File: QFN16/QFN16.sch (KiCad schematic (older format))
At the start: 4 parts, among them J1 Conn_01x08, J2 Conn_02x08_Counter_Clockwise, J3 Conn_01x08, J4 Conn_02x08_Counter_Clockwise

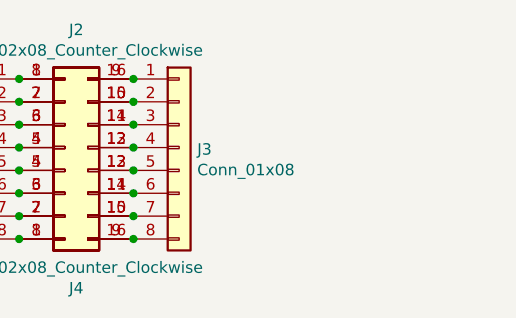
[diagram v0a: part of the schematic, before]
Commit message: Silkscreens and sizes updated
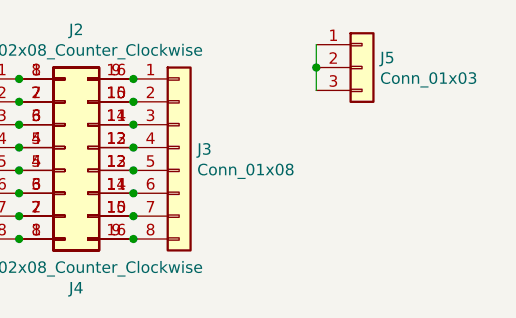
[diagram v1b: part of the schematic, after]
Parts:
- added J5: Conn_01x03, Connector_PinHeader_2.54mm:PinHeader_1x03_P2.54mm_Vertical, symbol Connector_Generic:Conn_01x03
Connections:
- new net: J5.1 (Pin_1), J5.2 (Pin_2), J5.3 (Pin_3)
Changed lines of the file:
@@
 Connection ~ 5800 3950
 Connection ~ 5800 4050
+$Comp
+L Connector_Generic:Conn_01x03 J5
+U 1 1 5D3B084D
+P 6800 3300
+F 0 "J5" H 6879 3342 50  0000 L CNN
+F 1 "Conn_01x03" H 6879 3252 50  0000 L CNN
+F 2 "Connector_PinHeader_2.54mm:PinHeader_1x03_P2.54mm_Vertical" H 6800 3300 50  0001 C CNN
+F 3 "~" H 6800 3300 50  0001 C CNN
+	1    6800 3300
+	1    0    0    -1
+$EndComp
+Wire Wire Line
+	6600 3200 6600 3300
+Connection ~ 6600 3300
+Wire Wire Line
+	6600 3300 6600 3400
 $EndSCHEMATC

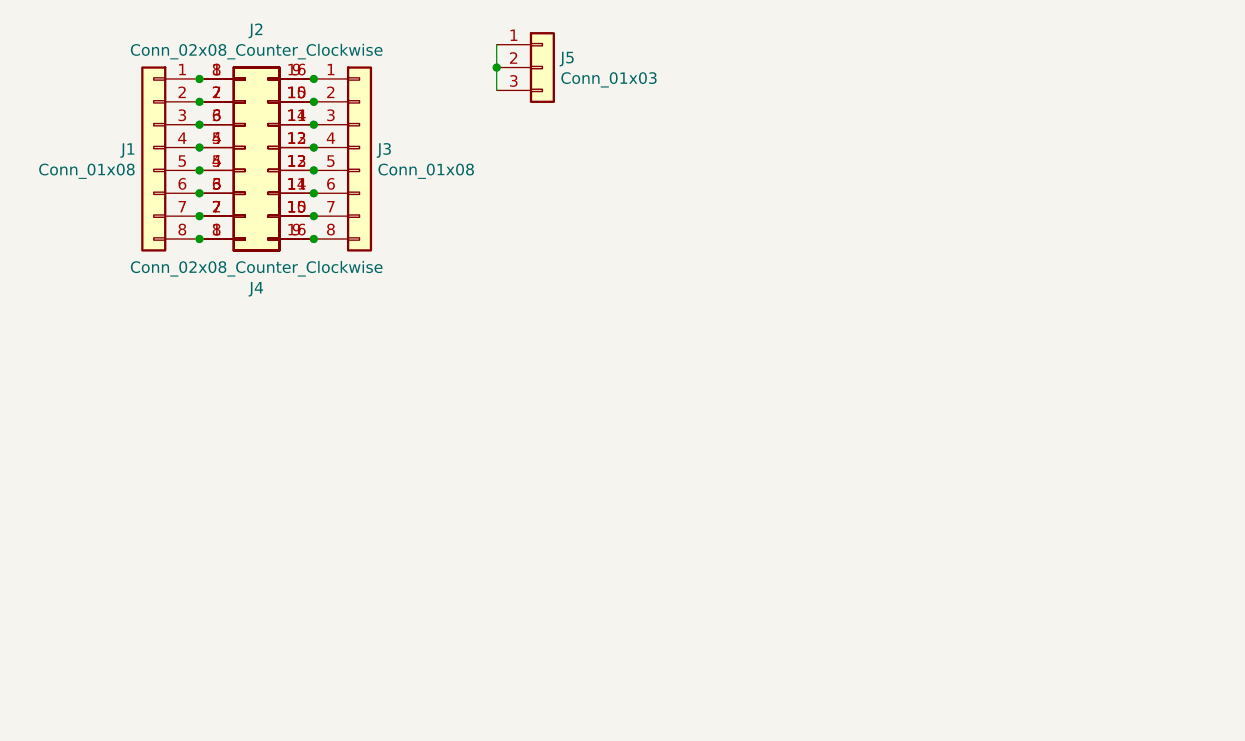
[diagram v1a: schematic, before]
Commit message: USB, SD and CR Cells Added
MicroSD, MicroUSB, MiniUSB, USB-C, CR1220, CR2032 added as well as all schematics page sizes optimised
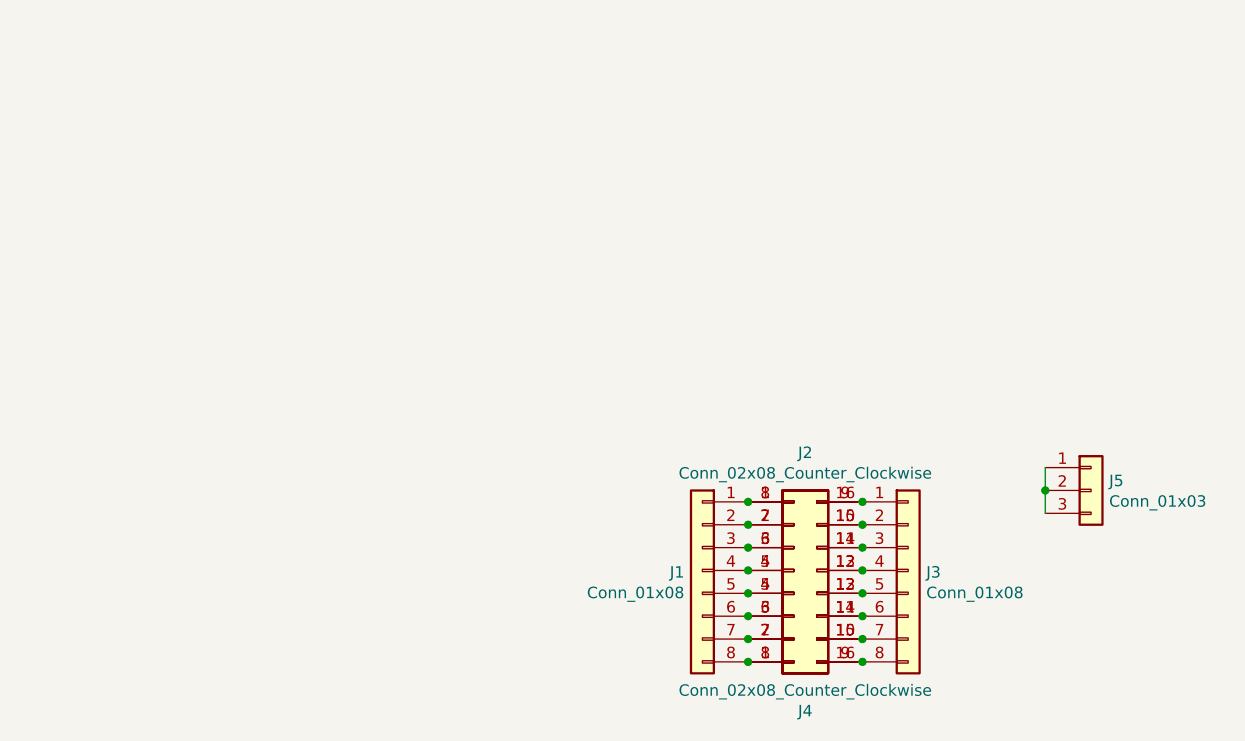
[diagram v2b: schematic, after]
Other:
- moved on the sheet: J1, J2, J3, J4, J5
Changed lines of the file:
@@
 encoding utf-8
 Sheet 1 1
-Title ""
-Date ""
-Rev ""
-Comp ""
-Comment1 ""
-Comment2 ""
-Comment3 ""
+Title "QFN16 to DIP Breakout Board"
+Date "2019-07-11"
+Rev "1"
+Comp "SirBoard"
+Comment1 "QFN16 P = 0.5mm"
+Comment2 "QFN16 P = 0.8mm"
+Comment3 "DIP16 P = 2.54mm"
 Comment4 ""
 $EndDescr
@@
 L Connector_Generic:Conn_01x08 J3
 U 1 1 5D27708E
-P 6000 3650
-F 0 "J3" H 6079 3642 50  0000 L CNN
-F 1 "Conn_01x08" H 6079 3552 50  0000 L CNN
-F 2 "Connector_PinHeader_2.54mm:PinHeader_1x08_P2.54mm_Vertical" H 6000 3650 50  0001 C CNN
-F 3 "~" H 6000 3650 50  0001 C CNN
-	1    6000 3650
+P 8400 5500
+F 0 "J3" H 8479 5492 50  0000 L CNN
+F 1 "Conn_01x08" H 8479 5402 50  0000 L CNN
+F 2 "Connector_PinHeader_2.54mm:PinHeader_1x08_P2.54mm_Vertical" H 8400 5500 50  0001 C CNN
+F 3 "~" H 8400 5500 50  0001 C CNN
+	1    8400 5500
 	1    0    0    -1
 $EndComp
@@
 L Connector_Generic:Conn_02x08_Counter_Clockwise J2
 U 1 1 5D2772F5
-P 5500 3650
-F 0 "J2" H 5550 4165 50  0000 C CNN
-F 1 "Conn_02x08_Counter_Clockwise" H 5550 4075 50  0000 C CNN
-F 2 "Package_DFN_QFN:QFN-20-1EP_4x4mm_P0.5mm_EP2.7x2.7mm" H 5500 3650 50  0001 C CNN
-F 3 "~" H 5500 3650 50  0001 C CNN
-	1    5500 3650
+P 7900 5500
+F 0 "J2" H 7950 6015 50  0000 C CNN
+F 1 "Conn_02x08_Counter_Clockwise" H 7950 5925 50  0000 C CNN
+F 2 "Package_DFN_QFN:QFN-20-1EP_4x4mm_P0.5mm_EP2.7x2.7mm" H 7900 5500 50  0001 C CNN
+F 3 "~" H 7900 5500 50  0001 C CNN
+	1    7900 5500
 	1    0    0    -1
 $EndComp
@@
 L Connector_Generic:Conn_01x08 J1
 U 1 1 5D27904E
-P 5100 3650
-F 0 "J1" H 5179 3642 50  0000 L CNN
-F 1 "Conn_01x08" H 5179 3552 50  0000 L CNN
-F 2 "Connector_PinHeader_2.54mm:PinHeader_1x08_P2.54mm_Vertical" H 5100 3650 50  0001 C CNN
-F 3 "~" H 5100 3650 50  0001 C CNN
-	1    5100 3650
+P 7500 5500
+F 0 "J1" H 7579 5492 50  0000 L CNN
+F 1 "Conn_01x08" H 7579 5402 50  0000 L CNN
+F 2 "Connector_PinHeader_2.54mm:PinHeader_1x08_P2.54mm_Vertical" H 7500 5500 50  0001 C CNN
+F 3 "~" H 7500 5500 50  0001 C CNN
+	1    7500 5500
 	-1   0    0    -1
 $EndComp
@@
 L Connector_Generic:Conn_02x08_Counter_Clockwise J4
 U 1 1 5D27A0A0
-P 5500 3750
-F 0 "J4" H 5550 4265 50  0000 C CNN
-F 1 "Conn_02x08_Counter_Clockwise" H 5550 4175 50  0000 C CNN
-F 2 "Package_DFN_QFN:QFN-16-1EP_5x5mm_P0.8mm_EP2.7x2.7mm" H 5500 3750 50  0001 C CNN
-F 3 "~" H 5500 3750 50  0001 C CNN
-	1    5500 3750
+P 7900 5600
+F 0 "J4" H 7950 6115 50  0000 C CNN
+F 1 "Conn_02x08_Counter_Clockwise" H 7950 6025 50  0000 C CNN
+F 2 "Package_DFN_QFN:QFN-16-1EP_5x5mm_P0.8mm_EP2.7x2.7mm" H 7900 5600 50  0001 C CNN
+F 3 "~" H 7900 5600 50  0001 C CNN
+	1    7900 5600
 	1    0    0    1
 $EndComp
-Connection ~ 5300 3350
-Connection ~ 5300 3450
-Connection ~ 5300 3550
-Connection ~ 5300 3650
-Connection ~ 5300 3750
-Connection ~ 5300 3850
-Connection ~ 5300 3950
-Connection ~ 5300 4050
-Connection ~ 5800 3350
-Connection ~ 5800 3450
-Connection ~ 5800 3550
-Connection ~ 5800 3650
-Connection ~ 5800 3750
-Connection ~ 5800 3850
-Connection ~ 5800 3950
-Connection ~ 5800 4050
+Connection ~ 7700 5200
+Connection ~ 7700 5300
+Connection ~ 7700 5400
+Connection ~ 7700 5500
+Connection ~ 7700 5600
+Connection ~ 7700 5700
+Connection ~ 7700 5800
+Connection ~ 7700 5900
+Connection ~ 8200 5200
+Connection ~ 8200 5300
+Connection ~ 8200 5400
+Connection ~ 8200 5500
+Connection ~ 8200 5600
+Connection ~ 8200 5700
+Connection ~ 8200 5800
+Connection ~ 8200 5900
 $Comp
 L Connector_Generic:Conn_01x03 J5
 U 1 1 5D3B084D
-P 6800 3300
-F 0 "J5" H 6879 3342 50  0000 L CNN
-F 1 "Conn_01x03" H 6879 3252 50  0000 L CNN
-F 2 "Connector_PinHeader_2.54mm:PinHeader_1x03_P2.54mm_Vertical" H 6800 3300 50  0001 C CNN
-F 3 "~" H 6800 3300 50  0001 C CNN
-	1    6800 3300
+P 9200 5150
+F 0 "J5" H 9279 5192 50  0000 L CNN
+F 1 "Conn_01x03" H 9279 5102 50  0000 L CNN
+F 2 "Connector_PinHeader_2.54mm:PinHeader_1x03_P2.54mm_Vertical" H 9200 5150 50  0001 C CNN
+F 3 "~" H 9200 5150 50  0001 C CNN
+	1    9200 5150
 	1    0    0    -1
 $EndComp
 Wire Wire Line
-	6600 3200 6600 3300
-Connection ~ 6600 3300
+	9000 5050 9000 5150
+Connection ~ 9000 5150
 Wire Wire Line
-	6600 3300 6600 3400
+	9000 5150 9000 5250
 $EndSCHEMATC

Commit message: Page Settings Updated
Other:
- moved on the sheet: J1, J2, J3, J4, J5
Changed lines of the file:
@@
 EELAYER 29 0
 EELAYER END
-$Descr A4 11693 8268
+$Descr User 8268 5807
 encoding utf-8
 Sheet 1 1
@@
 L Connector_Generic:Conn_01x08 J3
 U 1 1 5D27708E
-P 8400 5500
-F 0 "J3" H 8479 5492 50  0000 L CNN
-F 1 "Conn_01x08" H 8479 5402 50  0000 L CNN
-F 2 "Connector_PinHeader_2.54mm:PinHeader_1x08_P2.54mm_Vertical" H 8400 5500 50  0001 C CNN
-F 3 "~" H 8400 5500 50  0001 C CNN
-	1    8400 5500
+P 4525 2450
+F 0 "J3" H 4604 2442 50  0000 L CNN
+F 1 "Conn_01x08" H 4604 2352 50  0000 L CNN
+F 2 "Connector_PinHeader_2.54mm:PinHeader_1x08_P2.54mm_Vertical" H 4525 2450 50  0001 C CNN
+F 3 "~" H 4525 2450 50  0001 C CNN
+	1    4525 2450
 	1    0    0    -1
 $EndComp
@@
 L Connector_Generic:Conn_02x08_Counter_Clockwise J2
 U 1 1 5D2772F5
-P 7900 5500
-F 0 "J2" H 7950 6015 50  0000 C CNN
-F 1 "Conn_02x08_Counter_Clockwise" H 7950 5925 50  0000 C CNN
-F 2 "Package_DFN_QFN:QFN-20-1EP_4x4mm_P0.5mm_EP2.7x2.7mm" H 7900 5500 50  0001 C CNN
-F 3 "~" H 7900 5500 50  0001 C CNN
-	1    7900 5500
+P 4025 2450
+F 0 "J2" H 4075 2965 50  0000 C CNN
+F 1 "Conn_02x08_Counter_Clockwise" H 4075 2875 50  0000 C CNN
+F 2 "Package_DFN_QFN:QFN-20-1EP_4x4mm_P0.5mm_EP2.7x2.7mm" H 4025 2450 50  0001 C CNN
+F 3 "~" H 4025 2450 50  0001 C CNN
+	1    4025 2450
 	1    0    0    -1
 $EndComp
@@
 L Connector_Generic:Conn_01x08 J1
 U 1 1 5D27904E
-P 7500 5500
-F 0 "J1" H 7579 5492 50  0000 L CNN
-F 1 "Conn_01x08" H 7579 5402 50  0000 L CNN
-F 2 "Connector_PinHeader_2.54mm:PinHeader_1x08_P2.54mm_Vertical" H 7500 5500 50  0001 C CNN
-F 3 "~" H 7500 5500 50  0001 C CNN
-	1    7500 5500
+P 3625 2450
+F 0 "J1" H 3704 2442 50  0000 L CNN
+F 1 "Conn_01x08" H 3704 2352 50  0000 L CNN
+F 2 "Connector_PinHeader_2.54mm:PinHeader_1x08_P2.54mm_Vertical" H 3625 2450 50  0001 C CNN
+F 3 "~" H 3625 2450 50  0001 C CNN
+	1    3625 2450
 	-1   0    0    -1
 $EndComp
@@
 L Connector_Generic:Conn_02x08_Counter_Clockwise J4
 U 1 1 5D27A0A0
-P 7900 5600
-F 0 "J4" H 7950 6115 50  0000 C CNN
-F 1 "Conn_02x08_Counter_Clockwise" H 7950 6025 50  0000 C CNN
-F 2 "Package_DFN_QFN:QFN-16-1EP_5x5mm_P0.8mm_EP2.7x2.7mm" H 7900 5600 50  0001 C CNN
-F 3 "~" H 7900 5600 50  0001 C CNN
-	1    7900 5600
+P 4025 2550
+F 0 "J4" H 4075 3065 50  0000 C CNN
+F 1 "Conn_02x08_Counter_Clockwise" H 4075 2975 50  0000 C CNN
+F 2 "Package_DFN_QFN:QFN-16-1EP_5x5mm_P0.8mm_EP2.7x2.7mm" H 4025 2550 50  0001 C CNN
+F 3 "~" H 4025 2550 50  0001 C CNN
+	1    4025 2550
 	1    0    0    1
 $EndComp
-Connection ~ 7700 5200
-Connection ~ 7700 5300
-Connection ~ 7700 5400
-Connection ~ 7700 5500
-Connection ~ 7700 5600
-Connection ~ 7700 5700
-Connection ~ 7700 5800
-Connection ~ 7700 5900
-Connection ~ 8200 5200
-Connection ~ 8200 5300
-Connection ~ 8200 5400
-Connection ~ 8200 5500
-Connection ~ 8200 5600
-Connection ~ 8200 5700
-Connection ~ 8200 5800
-Connection ~ 8200 5900
+Connection ~ 3825 2150
+Connection ~ 3825 2250
+Connection ~ 3825 2350
+Connection ~ 3825 2450
+Connection ~ 3825 2550
+Connection ~ 3825 2650
+Connection ~ 3825 2750
+Connection ~ 3825 2850
+Connection ~ 4325 2150
+Connection ~ 4325 2250
+Connection ~ 4325 2350
+Connection ~ 4325 2450
+Connection ~ 4325 2550
+Connection ~ 4325 2650
+Connection ~ 4325 2750
+Connection ~ 4325 2850
 $Comp
 L Connector_Generic:Conn_01x03 J5
 U 1 1 5D3B084D
-P 9200 5150
-F 0 "J5" H 9279 5192 50  0000 L CNN
-F 1 "Conn_01x03" H 9279 5102 50  0000 L CNN
-F 2 "Connector_PinHeader_2.54mm:PinHeader_1x03_P2.54mm_Vertical" H 9200 5150 50  0001 C CNN
-F 3 "~" H 9200 5150 50  0001 C CNN
-	1    9200 5150
+P 5325 2100
+F 0 "J5" H 5404 2142 50  0000 L CNN
+F 1 "Conn_01x03" H 5404 2052 50  0000 L CNN
+F 2 "Connector_PinHeader_2.54mm:PinHeader_1x03_P2.54mm_Vertical" H 5325 2100 50  0001 C CNN
+F 3 "~" H 5325 2100 50  0001 C CNN
+	1    5325 2100
 	1    0    0    -1
 $EndComp
 Wire Wire Line
-	9000 5050 9000 5150
-Connection ~ 9000 5150
+	5125 2000 5125 2100
+Connection ~ 5125 2100
 Wire Wire Line
-	9000 5150 9000 5250
+	5125 2100 5125 2200
 $EndSCHEMATC

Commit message: Schematic PDF and 3D Renders added
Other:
- moved on the sheet: J1, J2, J3, J4, J5
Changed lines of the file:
@@
 EELAYER 29 0
 EELAYER END
-$Descr User 8268 5807
+$Descr User 5197 4016
 encoding utf-8
 Sheet 1 1
@@
 L Connector_Generic:Conn_01x08 J3
 U 1 1 5D27708E
-P 4525 2450
-F 0 "J3" H 4604 2442 50  0000 L CNN
-F 1 "Conn_01x08" H 4604 2352 50  0000 L CNN
-F 2 "Connector_PinHeader_2.54mm:PinHeader_1x08_P2.54mm_Vertical" H 4525 2450 50  0001 C CNN
-F 3 "~" H 4525 2450 50  0001 C CNN
-	1    4525 2450
+P 2825 1425
+F 0 "J3" H 2904 1417 50  0000 L CNN
+F 1 "Conn_01x08" H 2904 1327 50  0000 L CNN
+F 2 "Connector_PinHeader_2.54mm:PinHeader_1x08_P2.54mm_Vertical" H 2825 1425 50  0001 C CNN
+F 3 "~" H 2825 1425 50  0001 C CNN
+	1    2825 1425
 	1    0    0    -1
 $EndComp
@@
 L Connector_Generic:Conn_02x08_Counter_Clockwise J2
 U 1 1 5D2772F5
-P 4025 2450
-F 0 "J2" H 4075 2965 50  0000 C CNN
-F 1 "Conn_02x08_Counter_Clockwise" H 4075 2875 50  0000 C CNN
-F 2 "Package_DFN_QFN:QFN-20-1EP_4x4mm_P0.5mm_EP2.7x2.7mm" H 4025 2450 50  0001 C CNN
-F 3 "~" H 4025 2450 50  0001 C CNN
-	1    4025 2450
+P 2325 1425
+F 0 "J2" H 2375 1940 50  0000 C CNN
+F 1 "Conn_02x08_Counter_Clockwise" H 2375 1850 50  0000 C CNN
+F 2 "Package_DFN_QFN:QFN-20-1EP_4x4mm_P0.5mm_EP2.7x2.7mm" H 2325 1425 50  0001 C CNN
+F 3 "~" H 2325 1425 50  0001 C CNN
+	1    2325 1425
 	1    0    0    -1
 $EndComp
@@
 L Connector_Generic:Conn_01x08 J1
 U 1 1 5D27904E
-P 3625 2450
-F 0 "J1" H 3704 2442 50  0000 L CNN
-F 1 "Conn_01x08" H 3704 2352 50  0000 L CNN
-F 2 "Connector_PinHeader_2.54mm:PinHeader_1x08_P2.54mm_Vertical" H 3625 2450 50  0001 C CNN
-F 3 "~" H 3625 2450 50  0001 C CNN
-	1    3625 2450
+P 1925 1425
+F 0 "J1" H 2004 1417 50  0000 L CNN
+F 1 "Conn_01x08" H 2004 1327 50  0000 L CNN
+F 2 "Connector_PinHeader_2.54mm:PinHeader_1x08_P2.54mm_Vertical" H 1925 1425 50  0001 C CNN
+F 3 "~" H 1925 1425 50  0001 C CNN
+	1    1925 1425
 	-1   0    0    -1
 $EndComp
@@
 L Connector_Generic:Conn_02x08_Counter_Clockwise J4
 U 1 1 5D27A0A0
-P 4025 2550
-F 0 "J4" H 4075 3065 50  0000 C CNN
-F 1 "Conn_02x08_Counter_Clockwise" H 4075 2975 50  0000 C CNN
-F 2 "Package_DFN_QFN:QFN-16-1EP_5x5mm_P0.8mm_EP2.7x2.7mm" H 4025 2550 50  0001 C CNN
-F 3 "~" H 4025 2550 50  0001 C CNN
-	1    4025 2550
+P 2325 1525
+F 0 "J4" H 2375 2040 50  0000 C CNN
+F 1 "Conn_02x08_Counter_Clockwise" H 2375 1950 50  0000 C CNN
+F 2 "Package_DFN_QFN:QFN-16-1EP_5x5mm_P0.8mm_EP2.7x2.7mm" H 2325 1525 50  0001 C CNN
+F 3 "~" H 2325 1525 50  0001 C CNN
+	1    2325 1525
 	1    0    0    1
 $EndComp
-Connection ~ 3825 2150
-Connection ~ 3825 2250
-Connection ~ 3825 2350
-Connection ~ 3825 2450
-Connection ~ 3825 2550
-Connection ~ 3825 2650
-Connection ~ 3825 2750
-Connection ~ 3825 2850
-Connection ~ 4325 2150
-Connection ~ 4325 2250
-Connection ~ 4325 2350
-Connection ~ 4325 2450
-Connection ~ 4325 2550
-Connection ~ 4325 2650
-Connection ~ 4325 2750
-Connection ~ 4325 2850
+Connection ~ 2125 1125
+Connection ~ 2125 1225
+Connection ~ 2125 1325
+Connection ~ 2125 1425
+Connection ~ 2125 1525
+Connection ~ 2125 1625
+Connection ~ 2125 1725
+Connection ~ 2125 1825
+Connection ~ 2625 1125
+Connection ~ 2625 1225
+Connection ~ 2625 1325
+Connection ~ 2625 1425
+Connection ~ 2625 1525
+Connection ~ 2625 1625
+Connection ~ 2625 1725
+Connection ~ 2625 1825
 $Comp
 L Connector_Generic:Conn_01x03 J5
 U 1 1 5D3B084D
-P 5325 2100
-F 0 "J5" H 5404 2142 50  0000 L CNN
-F 1 "Conn_01x03" H 5404 2052 50  0000 L CNN
-F 2 "Connector_PinHeader_2.54mm:PinHeader_1x03_P2.54mm_Vertical" H 5325 2100 50  0001 C CNN
-F 3 "~" H 5325 2100 50  0001 C CNN
-	1    5325 2100
+P 3625 1075
+F 0 "J5" H 3704 1117 50  0000 L CNN
+F 1 "Conn_01x03" H 3704 1027 50  0000 L CNN
+F 2 "Connector_PinHeader_2.54mm:PinHeader_1x03_P2.54mm_Vertical" H 3625 1075 50  0001 C CNN
+F 3 "~" H 3625 1075 50  0001 C CNN
+	1    3625 1075
 	1    0    0    -1
 $EndComp
 Wire Wire Line
-	5125 2000 5125 2100
-Connection ~ 5125 2100
+	3425 975  3425 1075
+Connection ~ 3425 1075
 Wire Wire Line
-	5125 2100 5125 2200
+	3425 1075 3425 1175
 $EndSCHEMATC
